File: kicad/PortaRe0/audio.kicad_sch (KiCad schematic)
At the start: 49 parts, among them J2 SPK_R, J3 SPK_L, U11 RP2040#2, U13 PCM5102APWR, U14 TPA6132A2RTER, U15 MAX98357AEWL+T_R, U9 MAX98357AEWL+T_L, Y2 C70565

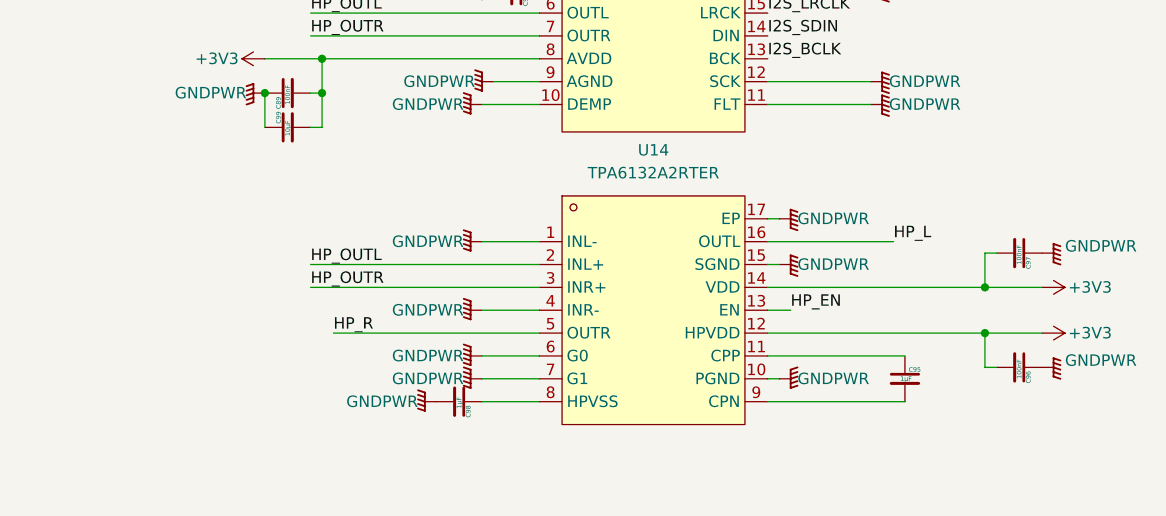
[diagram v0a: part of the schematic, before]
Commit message: KiCad/Docs: チェックシート09-10完了・回路修正(session27)
- 09_TPA6132A2: 入力ピン接続逆転修正(INL-/INR-が信号入力)
  ACカップリング2.2µF / EMIフィルタ470Ω+2.2nF / G0=+3V3(0dB) / HPVDD→2.2µF
- 10_TPS2042BDR_USBLC6: 全ピンOK・修正なし
- チェックシート照合 全10IC完了 → Phase 3 PCBレイアウトへ
- PROGRESS.md / index.md 更新

Co-Authored-By: Claude Sonnet 4.6 <noreply@anthropic.com>
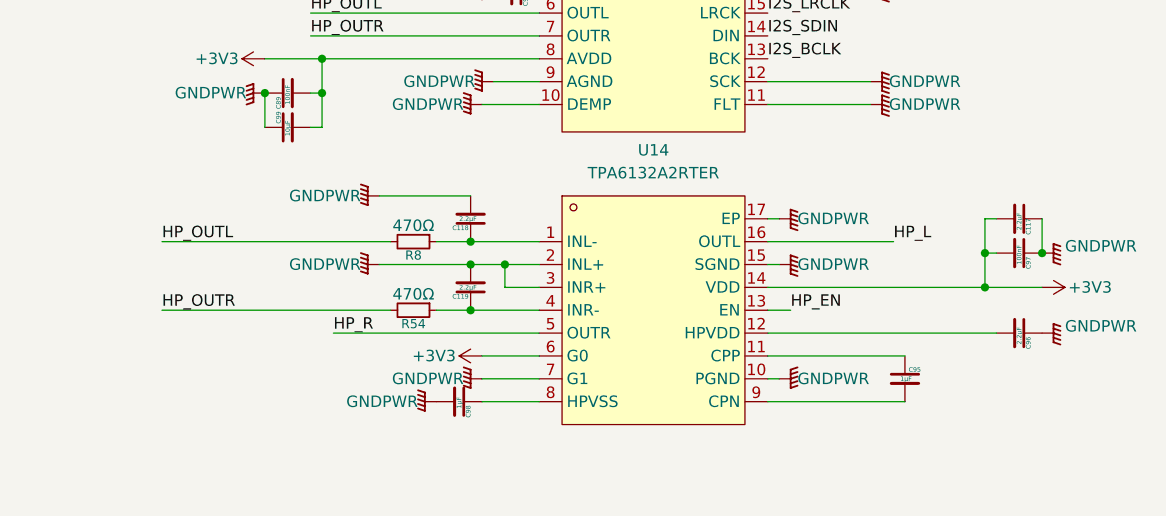
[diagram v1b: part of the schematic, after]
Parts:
- added C117, C118, C119: 2.2μF, symbol Device:C_Small
- added R54, R8: 470Ω, symbol Device:R_Small
- C96: value 100nF -> 2.2μF
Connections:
- net +3V3: now also U14.6 (G0), C117.2; no longer C96.2, U14.12 (HPVDD)
- net GNDPWR: now also U14.2 (INL+), U14.3 (INR+), C117.1, C118.2, C119.2; no longer U14.1 (INL-), U14.4 (INR-), U14.6 (G0)
- net HP_OUTL: now also R8.2; no longer U14.2 (INL+)
- net HP_OUTR: now also R54.2; no longer U14.3 (INR+)
- new net: C118.1, R8.1, U14.1 (INL-)
- new net: C119.1, R54.1, U14.4 (INR-)
- new net: C96.2, U14.12 (HPVDD)
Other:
- moved on the sheet: C96

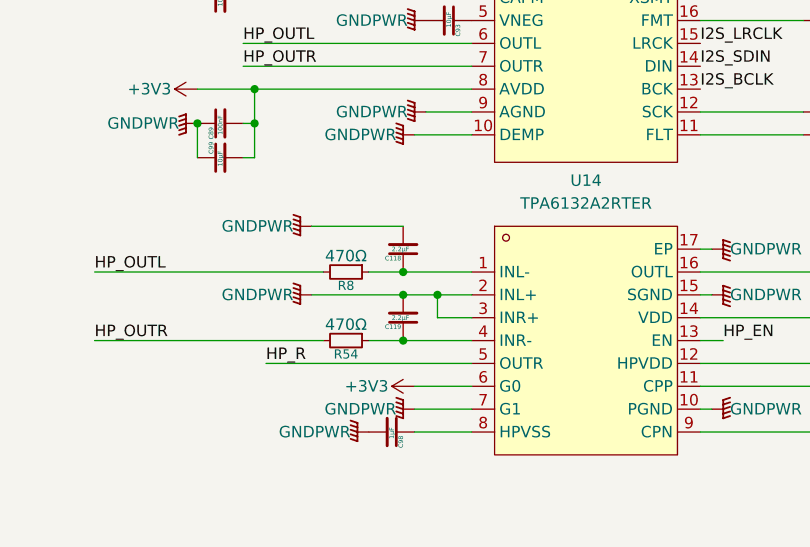
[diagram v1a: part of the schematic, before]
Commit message: Docs/KiCad: session29終了処理・LED/スイッチ確定・audio/power修正
Co-Authored-By: Claude Sonnet 4.6 <noreply@anthropic.com>
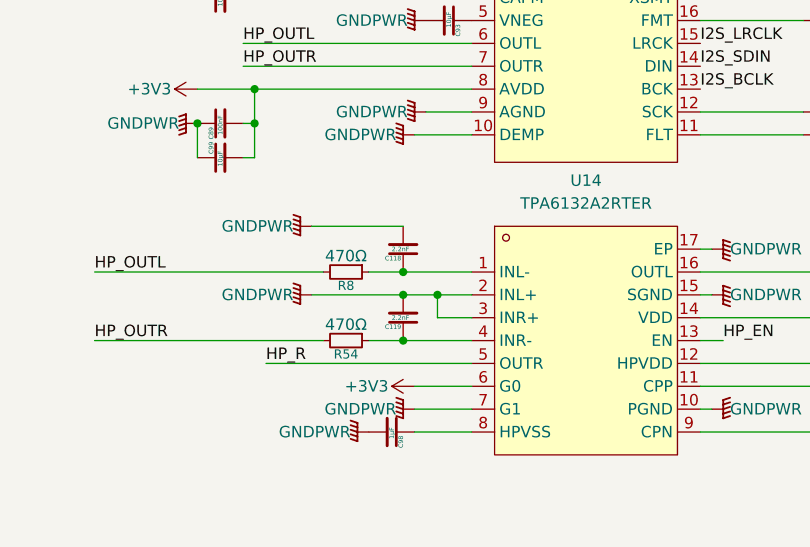
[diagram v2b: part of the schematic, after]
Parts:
- C118, C119: value 2.2μF -> 2.2nF
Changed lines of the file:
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@@
 			)
 		)
-		(property "Value" "2.2μF"
+		(property "Value" "2.2nF"
 			(at 209.55 153.67 0)
 			(effects
@@
 			)
 		)
-		(property "Value" "2.2μF"
+		(property "Value" "2.2nF"
 			(at 209.55 161.29 0)
 			(effects

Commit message: KiCad/Docs: session30終了処理・フットプリント割り当て完了・コネクタ確定
- フットプリント全割り当て完了（全シート）
- 新規フットプリント追加: SKSCLBE010/SKRPABE010/クリスタル/インダクタ×3/JST PHコネクタ×2
- コネクタ確定: バッテリー=B8B-PH-K-S(C157974) / SPK+FAN=B2B-PH-K-S(C131337)
- J5(hdmi_adapter): PinHeader_2x08_P2.00mm_Vertical
- Claude.md: ファン制御 RP2040 #1 GP26→BSS138→J6 に更新
- passive_parts.txt: コネクタセクション追加

Co-Authored-By: Claude Sonnet 4.6 <noreply@anthropic.com>
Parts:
- C115, C116, C117, C118, C119, C70, C71, C72, C73, C74, C75, C76, C77, C78, C79, C80, C81, C82, C83, C84, C85, C86, C87, C88, C89, C90, C91, C92, C93, C94, C95, C96, C97, C98, C99: footprint (none) -> Capacitor_SMD:C_0603_1608Metric
- J2, J3: footprint (none) -> PortaRe0:CONN-TH_B2B-PH-K-S
- K_SW65: footprint (none) -> PortaRe0:KEY-SMD_4P-L4.2-W3.2-P2.20-LS4.6
- R35, R36, R37, R38, R39, R40, R41, R54, R8: footprint (none) -> Resistor_SMD:R_0603_1608Metric
- Y2: footprint (none) -> PortaRe0:CRYSTAL-SMD_4P-L3.2-W2.5-BL
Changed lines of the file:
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@@
 			)
 		)
-		(property "Footprint" ""
+		(property "Footprint" "Capacitor_SMD:C_0603_1608Metric"
 			(at 176.53 63.5 0)
 			(effects
@@
 			)
 		)
-		(property "Footprint" ""
+		(property "Footprint" "Capacitor_SMD:C_0603_1608Metric"
 			(at 210.82 153.67 0)
 			(effects
@@
 			)
 		)
-		(property "Footprint" ""
+		(property "Footprint" "Capacitor_SMD:C_0603_1608Metric"
 			(at 271.78 153.67 0)
 			(effects
@@
 			)
 		)
-		(property "Footprint" ""
+		(property "Footprint" "Capacitor_SMD:C_0603_1608Metric"
 			(at 114.3 72.39 0)
 			(effects
@@
 			)
 		)
-		(property "Footprint" ""
+		(property "Footprint" "Capacitor_SMD:C_0603_1608Metric"
 			(at 97.79 63.5 0)
 			(effects
@@
 			)
 		)
-		(property "Footprint" ""
+		(property "Footprint" "Capacitor_SMD:C_0603_1608Metric"
 			(at 182.88 63.5 0)
 			(effects
@@
 			)
 		)
-		(property "Footprint" ""
+		(property "Footprint" "Capacitor_SMD:C_0603_1608Metric"
 			(at 190.5 125.73 0)
 			(effects
@@
 			)
 		)
-		(property "Footprint" ""
+		(property "Footprint" "Capacitor_SMD:C_0603_1608Metric"
 			(at 92.71 63.5 0)
 			(effects
@@
 			)
 		)
-		(property "Footprint" ""
+		(property "Footprint" "PortaRe0:CRYSTAL-SMD_4P-L3.2-W2.5-BL"
 			(at 53.34 134.62 0)
 			(effects
@@
 			)
 		)
-		(property "Footprint" ""
+		(property "Footprint" "Capacitor_SMD:C_0603_1608Metric"
 			(at 252.73 123.19 0)
 			(effects
@@
 			)
 		)
-		(property "Footprint" ""
+		(property "Footprint" "Capacitor_SMD:C_0603_1608Metric"
 			(at 95.25 63.5 0)
 			(effects
@@
 			)
 		)
-		(property "Footprint" ""
+		(property "Footprint" "Capacitor_SMD:C_0603_1608Metric"
 			(at 194.31 91.44 0)
 			(effects
@@
 			)
 		)
-		(property "Footprint" ""
+		(property "Footprint" "Capacitor_SMD:C_0603_1608Metric"
 			(at 190.5 143.51 0)
 			(effects
@@
 			)
 		)
-		(property "Footprint" ""
+		(property "Footprint" "Capacitor_SMD:C_0603_1608Metric"
 			(at 48.26 137.16 0)
 			(effects
@@
 			)
 		)
-		(property "Footprint" ""
+		(property "Footprint" "PortaRe0:CONN-TH_B2B-PH-K-S"
 			(at 262.89 102.87 0)
 			(effects
@@
 			)
 		)
-		(property "Footprint" ""
+		(property "Footprint" "Capacitor_SMD:C_0603_1608Metric"
 			(at 76.2 63.5 0)
 			(effects
@@
 			)
 		)
-		(property "Footprint" ""
+		(property "Footprint" "Resistor_SMD:R_0603_1608Metric"
 			(at 54.61 149.86 0)
 			(effects
@@
 			)
 		)
-		(property "Footprint" ""
+		(property "Footprint" "Resistor_SMD:R_0603_1608Metric"
 			(at 130.81 86.36 0)
 			(effects
@@
 			)
 		)
-		(property "Footprint" ""
+		(property "Footprint" "Capacitor_SMD:C_0603_1608Metric"
 			(at 187.96 91.44 0)
 			(effects
@@
 			)
 		)
-		(property "Footprint" ""
+		(property "Footprint" "Resistor_SMD:R_0603_1608Metric"
 			(at 130.81 88.9 0)
 			(effects
@@
 			)
 		)
-		(property "Footprint" ""
+		(property "Footprint" "PortaRe0:KEY-SMD_4P-L4.2-W3.2-P2.20-LS4.6"
 			(at 44.45 87.63 0)
 			(effects
@@
 			)
 		)
-		(property "Footprint" ""
+		(property "Footprint" "Capacitor_SMD:C_0603_1608Metric"
 			(at 210.82 161.29 0)
 			(effects
@@
 			)
 		)
-		(property "Footprint" ""
+		(property "Footprint" "Capacitor_SMD:C_0603_1608Metric"
 			(at 106.68 63.5 0)
 			(effects
@@
 			)
 		)
-		(property "Footprint" ""
+		(property "Footprint" "Capacitor_SMD:C_0603_1608Metric"
 			(at 190.5 121.92 0)
 			(effects
@@
 			)
 		)
-		(property "Footprint" ""
+		(property "Footprint" "Resistor_SMD:R_0603_1608Metric"
 			(at 204.47 156.21 0)
 			(effects
@@
 			)
 		)
-		(property "Footprint" ""
+		(property "Footprint" "Capacitor_SMD:C_0603_1608Metric"
 			(at 190.5 139.7 0)
 			(effects
@@
 			)
 		)
-		(property "Footprint" ""
+		(property "Footprint" "Capacitor_SMD:C_0603_1608Metric"
 			(at 271.78 166.37 0)
 			(effects
@@
 			)
 		)
-		(property "Footprint" ""
+		(property "Footprint" "Capacitor_SMD:C_0603_1608Metric"
 			(at 215.9 128.27 0)
 			(effects
@@
 			)
 		)
-		(property "Footprint" ""
+		(property "Footprint" "Capacitor_SMD:C_0603_1608Metric"
 			(at 102.87 63.5 0)
 			(effects
@@
 			)
 		)
-		(property "Footprint" ""
+		(property "Footprint" "Capacitor_SMD:C_0603_1608Metric"
 			(at 259.08 171.45 0)
 			(effects
@@
 			)
 		)
-		(property "Footprint" ""
+		(property "Footprint" "Capacitor_SMD:C_0603_1608Metric"
 			(at 48.26 132.08 0)
 			(effects
@@
 			)
 		)
-		(property "Footprint" ""
+		(property "Footprint" "Capacitor_SMD:C_0603_1608Metric"
 			(at 73.66 63.5 0)
 			(effects
@@
 			)
 		)
-		(property "Footprint" ""
+		(property "Footprint" "Capacitor_SMD:C_0603_1608Metric"
 			(at 271.78 121.92 0)
 			(effects
@@
 			)
 		)
-		(property "Footprint" ""
+		(property "Footprint" "Capacitor_SMD:C_0603_1608Metric"
 			(at 81.28 63.5 0)
 			(effects
@@
 			)
 		)
-		(property "Footprint" ""
+		(property "Footprint" "Resistor_SMD:R_0603_1608Metric"
 			(at 207.01 64.77 0)
 			(effects
@@
 			)
 		)
-		(property "Footprint" ""
+		(property "Footprint" "Resistor_SMD:R_0603_1608Metric"
 			(at 110.49 72.39 0)
 			(effects
@@
 			)
 		)
-		(property "Footprint" ""
+		(property "Footprint" "Capacitor_SMD:C_0603_1608Metric"
 			(at 271.78 157.48 0)
 			(effects
@@
 			)
 		)
-		(property "Footprint" ""
+		(property "Footprint" "Capacitor_SMD:C_0603_1608Metric"
 			(at 100.33 63.5 0)
 			(effects
@@
 			)
 		)
-		(property "Footprint" ""
+		(property "Footprint" "Resistor_SMD:R_0603_1608Metric"
 			(at 113.03 44.45 0)
 			(effects
@@
 			)
 		)
-		(property "Footprint" ""
+		(property "Footprint" "Resistor_SMD:R_0603_1608Metric"
 			(at 58.42 97.79 0)
 			(effects
@@
 			)
 		)
-		(property "Footprint" ""
+		(property "Footprint" "Capacitor_SMD:C_0603_1608Metric"
 			(at 85.09 63.5 0)
 			(effects
@@
 			)
 		)
-		(property "Footprint" ""
+		(property "Footprint" "Capacitor_SMD:C_0603_1608Metric"
 			(at 76.2 41.91 0)
 			(effects
@@
 			)
 		)
-		(property "Footprint" ""
+		(property "Footprint" "Resistor_SMD:R_0603_1608Metric"
 			(at 204.47 163.83 0)
 			(effects
@@
 			)
 		)
-		(property "Footprint" ""
+		(property "Footprint" "Capacitor_SMD:C_0603_1608Metric"
 			(at 203.2 123.19 0)
 			(effects
@@
 			)
 		)
-		(property "Footprint" ""
+		(property "Footprint" "PortaRe0:CONN-TH_B2B-PH-K-S"
 			(at 265.43 74.93 0)
 			(effects
@@
 			)
 		)
-		(property "Footprint" ""
+		(property "Footprint" "Capacitor_SMD:C_0603_1608Metric"
 			(at 271.78 125.73 0)
 			(effects
@@
 			)
 		)
-		(property "Footprint" ""
+		(property "Footprint" "Capacitor_SMD:C_0603_1608Metric"
 			(at 209.55 173.99 0)
 			(effects
@@
 			)
 		)
-		(property "Footprint" ""
+		(property "Footprint" "Capacitor_SMD:C_0603_1608Metric"
 			(at 90.17 63.5 0)
 			(effects

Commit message: Docs/KiCad: session31終了処理・PROGRESS/index更新
- キルスイッチ確定: MSK12C02(C431540) EN制御方式・KiCad配線完了
- ヘッドフォンジャック確定: PJ-307C(C16684) TH / 配線・pull-up完了
- J4バッテリーコネクタ: S8B-PH-K-S-LF-SN(C157915) 水平型確定
- BOM Y4フットプリント修正
- 新規ライブラリ追加: MSK12C02/PJ-307C/S8B-PH-K-S他
- Phase 2 回路設計 全シート完了

Co-Authored-By: Claude Sonnet 4.6 <noreply@anthropic.com>
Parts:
- added J9: PJ-307C, PortaRe0:AUDIO-TH_PJ307C, symbol PortaRe0:PJ-307C
- added R63: 100kΩ, Resistor_SMD:R_0603_1608Metric, symbol Device:R_Small
- J2, J3: footprint PortaRe0:CONN-TH_B2B-PH-K-S -> PortaRe0:CONN-TH_S2B-PH-K-S-LF-SN
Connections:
- net +3V3: now also R63.2
- net GNDPWR: now also J9.1
- net HP_DET: now also J9.4, R63.1
- net HP_L: now also J9.2
- net HP_R: now also J9.5
- no-connect marks 27 -> 28
